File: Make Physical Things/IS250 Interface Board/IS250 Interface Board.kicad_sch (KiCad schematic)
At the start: 6 parts, among them J1 24_Pin_Reorg, J2 16_Pin, J3 Barrel_Jack, SW1 SW_SPST, SW2 SW_MEC_5G

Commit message: Updated Components to have footprints
Added footprints to components that had the wrong ones or were completely missing
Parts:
- J1: footprint (none) -> IS250 Interface Board:24Pin
- J2: footprint (none) -> IS250 Interface Board:16Pin
- J3: footprint (none) -> Connector_BarrelJack:BarrelJack_Horizontal
- SW1: footprint (none) -> IS250 Interface Board:JaycarSlideSwitch
- SW2: footprint (none) -> Button_Switch_THT:SW_Tactile_SPST_Angled_PTS645Vx58-2LFS
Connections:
- net +12V: now also SW1.2 (B); no longer SW1.1 (A)
- net at J1.12 (IGN-SW): now also SW1.1 (A); no longer SW1.2 (B)

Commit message: Added components to PCB
Got all the components adding onto the PCB, and fixed pinname errors with the 2907
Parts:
- XA1: footprint (none) -> Arduino:Arduino_Mega2560_Shield
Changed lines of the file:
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@@
       (effects (font (size 1.524 1.524)))
     )
-    (property "Footprint" "" (id 2) (at 71.12 29.972 0)
+    (property "Footprint" "Arduino:Arduino_Mega2560_Shield" (id 2) (at 71.12 29.972 0)
       (effects (font (size 1.524 1.524)) hide)
     )
@@
     )
     (path "/befd90f1-e350-4c6b-9126-156e7cfd54fd/f532fa97-167c-4bca-bcaf-4a540362fc1c"
-      (reference "RV1") (unit 1) (value "R_Potentiometer") (footprint "")
+      (reference "RV1") (unit 1) (value "R_Potentiometer") (footprint "Potentiometer_THT:Potentiometer_Bourns_3386P_Vertical")
     )
     (path "/67c25448-ea3e-4950-a82a-fe1f009b9ce6"
@@
     )
     (path "/c10fe882-d0c6-4d01-8105-c15a551b4c6b/ee4a6612-4d72-41b2-94a6-c292d4d5cb83"
-      (reference "U2") (unit 1) (value "4017") (footprint "")
+      (reference "U2") (unit 1) (value "4017") (footprint "Package_DIP:DIP-16_W7.62mm")
     )
     (path "/49f3a792-f9d7-417d-ae9d-443f600ad87b"
-      (reference "XA1") (unit 1) (value "Arduino_Mega2560_Shield") (footprint "")
-    )
-  )
+      (reference "XA1") (unit 1) (value "Arduino_Mega2560_Shield") (footprint "Arduino:Arduino_Mega2560_Shield")
+    )
+  )

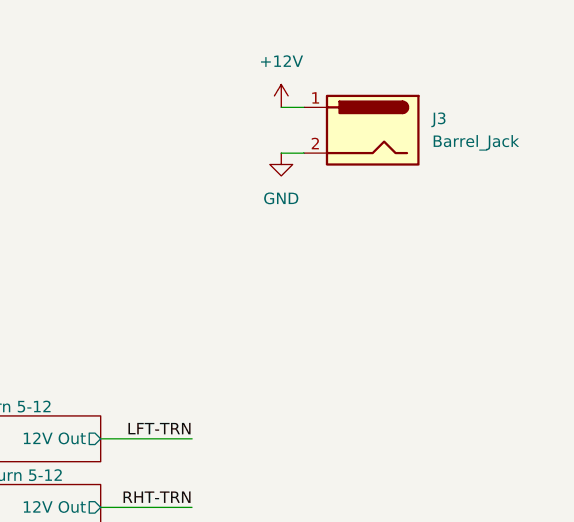
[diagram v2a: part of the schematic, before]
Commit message: Added XT60 and backup fuel resistor
Added an XT60 power connector, and an optional resistor if there isn't an AD8400 connected, so that the fuel gauge will show not empty
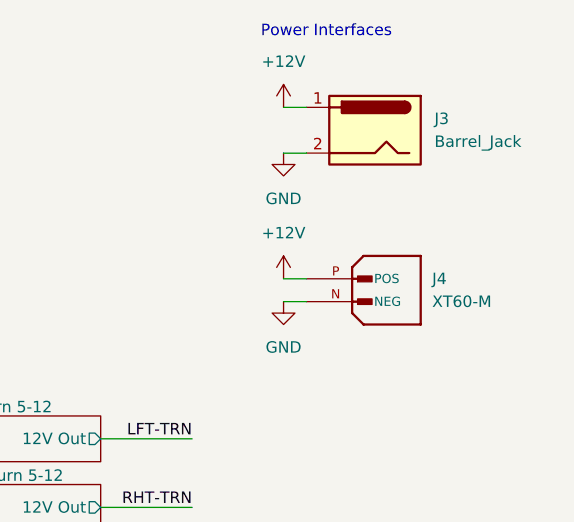
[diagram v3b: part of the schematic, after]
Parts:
- added J4: XT60-M, AMASS_XT60-M, symbol XT60-M:XT60-M
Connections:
- net +12V: now also J4.P (POS)
- net GND: now also J4.N (NEG)
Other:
- note added: "Power Interfaces"
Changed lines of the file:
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@@
-    (stroke (width 0) (type default) (color 0 0 0 0))
-  )
-  (wire (pts (xy 256.286 36.83) (xy 258.826 36.83))
     (stroke (width 0) (type default) (color 0 0 0 0))
   )
@@
     (stroke (width 0) (type default) (color 0 0 0 0))
   )
+  (wire (pts (xy 256.54 36.83) (xy 259.08 36.83))
+    (stroke (width 0) (type default) (color 0 0 0 0))
+  )
   (wire (pts (xy 106.68 60.452) (xy 116.586 60.452))
     (stroke (width 0) (type default) (color 0 0 0 0))
@@
     (stroke (width 0) (type default) (color 0 0 0 0))
   )
-  (wire (pts (xy 256.286 31.75) (xy 258.826 31.75))
+  (wire (pts (xy 256.54 31.75) (xy 259.08 31.75))
     (stroke (width 0) (type default) (color 0 0 0 0))
   )
@@
     (stroke (width 0) (type default) (color 0 0 0 0))
   )
+  (wire (pts (xy 256.54 50.8) (xy 259.08 50.8))
+    (stroke (width 0) (type default) (color 0 0 0 0))
+  )
   (wire (pts (xy 128.778 80.772) (xy 129.794 80.772))
     (stroke (width 0) (type default) (color 0 0 0 0))
@@
     (stroke (width 0) (type default) (color 0 0 0 0))
   )
+  (wire (pts (xy 256.54 53.34) (xy 259.08 53.34))
+    (stroke (width 0) (type default) (color 0 0 0 0))
+  )
   (wire (pts (xy 165.354 70.612) (xy 166.878 70.612))
     (stroke (width 0) (type default) (color 0 0 0 0))
@@
   (wire (pts (xy 121.158 77.47) (xy 121.158 83.566))
     (stroke (width 0) (type default) (color 0 0 0 0))
+  )
+  (text "Power Interfaces\n" (at 254 24.13 0)
+    (effects (font (size 1.27 1.27)) (justify left bottom))
   )
   (label "LFT-T" (at 93.218 116.332 180)
@@
     (effects (font (size 1.27 1.27)) (justify right bottom))
   )
-  (symbol (lib_id "power:+12V") (at 256.286 31.75 0) (unit 1)
-    (in_bom yes) (on_board yes) (fields_autoplaced)
-    (property "Reference" "#PWR0108" (id 0) (at 256.286 35.56 0)
-      (effects (font (size 1.27 1.27)) hide)
-    )
-    (property "Value" "+12V" (id 1) (at 256.286 26.67 0))
-    (property "Footprint" "" (id 2) (at 256.286 31.75 0)
-      (effects (font (size 1.27 1.27)) hide)
-    )
-    (property "Datasheet" "" (id 3) (at 256.286 31.75 0)
+  (symbol (lib_id "power:+12V") (at 256.54 31.75 0) (unit 1)
+    (in_bom yes) (on_board yes) (fields_autoplaced)
+    (property "Reference" "#PWR0108" (id 0) (at 256.54 35.56 0)
+      (effects (font (size 1.27 1.27)) hide)
+    )
+    (property "Value" "+12V" (id 1) (at 256.54 26.67 0))
+    (property "Footprint" "" (id 2) (at 256.54 31.75 0)
+      (effects (font (size 1.27 1.27)) hide)
+    )
+    (property "Datasheet" "" (id 3) (at 256.54 31.75 0)
       (effects (font (size 1.27 1.27)) hide)
     )
@@
     )
     (pin "1")
+  )
+  (symbol (lib_id "XT60-M:XT60-M") (at 264.16 53.34 0) (unit 1)
+    (in_bom yes) (on_board yes) (fields_autoplaced)
+    (property "Reference" "J4" (id 0) (at 273.05 50.7999 0)
+      (effects (font (size 1.27 1.27)) (justify left))
+    )
+    (property "Value" "XT60-M" (id 1) (at 273.05 53.3399 0)
+      (effects (font (size 1.27 1.27)) (justify left))
+    )
+    (property "Footprint" "AMASS_XT60-M" (id 2) (at 264.16 53.34 0)
+      (effects (font (size 1.27 1.27)) (justify left bottom) hide)
+    )
+    (property "Datasheet" "" (id 3) (at 264.16 53.34 0)
+      (effects (font (size 1.27 1.27)) (justify left bottom) hide)
+    )
+    (property "MAXIMUM_PACKAGE_HEIGHT" "16.00 mm" (id 4) (at 264.16 53.34 0)
+      (effects (font (size 1.27 1.27)) (justify left bottom) hide)
+    )
+    (property "MANUFACTURER" "AMASS" (id 5) (at 264.16 53.34 0)
+      (effects (font (size 1.27 1.27)) (justify left bottom) hide)
+    )
+    (property "PARTREV" "V1.2" (id 6) (at 264.16 53.34 0)
+      (effects (font (size 1.27 1.27)) (justify left bottom) hide)
+    )
+    (property "STANDARD" "IPC 7351B" (id 7) (at 264.16 53.34 0)
+      (effects (font (size 1.27 1.27)) (justify left bottom) hide)
+    )
+    (pin "N")
+    (pin "P")
   )
   (symbol (lib_id "Switch:SW_MEC_5G") (at 177.038 85.852 0) (unit 1)
@@
     (pin "2")
   )
-  (symbol (lib_id "power:GND") (at 256.286 36.83 0) (unit 1)
-    (in_bom yes) (on_board yes) (fields_autoplaced)
-    (property "Reference" "#PWR0107" (id 0) (at 256.286 43.18 0)
-      (effects (font (size 1.27 1.27)) hide)
-    )
-    (property "Value" "GND" (id 1) (at 256.286 41.91 0))
-    (property "Footprint" "" (id 2) (at 256.286 36.83 0)
-      (effects (font (size 1.27 1.27)) hide)
-    )
-    (property "Datasheet" "" (id 3) (at 256.286 36.83 0)
-      (effects (font (size 1.27 1.27)) hide)
-    )
-    (pin "1")
-  )
-  (symbol (lib_id "Connector:Barrel_Jack") (at 266.446 34.29 0) (mirror y) (unit 1)
-    (in_bom yes) (on_board yes) (fields_autoplaced)
-    (property "Reference" "J3" (id 0) (at 273.05 33.0199 0)
-      (effects (font (size 1.27 1.27)) (justify right))
-    )
-    (property "Value" "Barrel_Jack" (id 1) (at 273.05 35.5599 0)
-      (effects (font (size 1.27 1.27)) (justify right))
-    )
-    (property "Footprint" "Connector_BarrelJack:BarrelJack_Horizontal" (id 2) (at 265.176 35.306 0)
-      (effects (font (size 1.27 1.27)) hide)
-    )
-    (property "Datasheet" "~" (id 3) (at 265.176 35.306 0)
+  (symbol (lib_id "power:GND") (at 256.54 53.34 0) (unit 1)
+    (in_bom yes) (on_board yes) (fields_autoplaced)
+    (property "Reference" "#PWR0133" (id 0) (at 256.54 59.69 0)
+      (effects (font (size 1.27 1.27)) hide)
+    )
+    (property "Value" "GND" (id 1) (at 256.54 58.42 0))
+    (property "Footprint" "" (id 2) (at 256.54 53.34 0)
+      (effects (font (size 1.27 1.27)) hide)
+    )
+    (property "Datasheet" "" (id 3) (at 256.54 53.34 0)
+      (effects (font (size 1.27 1.27)) hide)
+    )
+    (pin "1")
+  )
+  (symbol (lib_id "power:GND") (at 256.54 36.83 0) (unit 1)
+    (in_bom yes) (on_board yes) (fields_autoplaced)
+    (property "Reference" "#PWR0107" (id 0) (at 256.54 43.18 0)
+      (effects (font (size 1.27 1.27)) hide)
+    )
+    (property "Value" "GND" (id 1) (at 256.54 41.91 0))
+    (property "Footprint" "" (id 2) (at 256.54 36.83 0)
+      (effects (font (size 1.27 1.27)) hide)
+    )
+    (property "Datasheet" "" (id 3) (at 256.54 36.83 0)
+      (effects (font (size 1.27 1.27)) hide)
+    )
+    (pin "1")
+  )
+  (symbol (lib_id "power:+12V") (at 256.54 50.8 0) (unit 1)
+    (in_bom yes) (on_board yes) (fields_autoplaced)
+    (property "Reference" "#PWR0134" (id 0) (at 256.54 54.61 0)
+      (effects (font (size 1.27 1.27)) hide)
+    )
+    (property "Value" "+12V" (id 1) (at 256.54 45.72 0))
+    (property "Footprint" "" (id 2) (at 256.54 50.8 0)
+      (effects (font (size 1.27 1.27)) hide)
+    )
+    (property "Datasheet" "" (id 3) (at 256.54 50.8 0)
+      (effects (font (size 1.27 1.27)) hide)
+    )
+    (pin "1")
+  )
+  (symbol (lib_id "Connector:Barrel_Jack") (at 266.7 34.29 0) (mirror y) (unit 1)
+    (in_bom yes) (on_board yes) (fields_autoplaced)
+    (property "Reference" "J3" (id 0) (at 273.304 33.0199 0)
+      (effects (font (size 1.27 1.27)) (justify right))
+    )
+    (property "Value" "Barrel_Jack" (id 1) (at 273.304 35.5599 0)
+      (effects (font (size 1.27 1.27)) (justify right))
+    )
+    (property "Footprint" "Connector_BarrelJack:BarrelJack_Horizontal" (id 2) (at 265.43 35.306 0)
+      (effects (font (size 1.27 1.27)) hide)
+    )
+    (property "Datasheet" "~" (id 3) (at 265.43 35.306 0)
       (effects (font (size 1.27 1.27)) hide)
     )
@@
       (reference "#PWR0132") (unit 1) (value "+12V") (footprint "")
     )
+    (path "/6a6f2c78-ccc0-41fa-beba-1d8264551389"
+      (reference "#PWR0133") (unit 1) (value "GND") (footprint "")
+    )
+    (path "/8595ee52-f88c-4dfe-a3e8-64a4bc6cf3ba"
+      (reference "#PWR0134") (unit 1) (value "+12V") (footprint "")
+    )
     (path "/b4ad7ea6-c60f-4c23-983b-e568869cc5ae"
       (reference "J1") (unit 1) (value "24_Pin_Reorg") (footprint "IS250 Interface Board:24Pin")
@@
       (reference "J3") (unit 1) (value "Barrel_Jack") (footprint "Connector_BarrelJack:BarrelJack_Horizontal")
     )
+    (path "/31965dda-df71-4f19-aaa7-a9c32fd53870"
+      (reference "J4") (unit 1) (value "XT60-M") (footprint "AMASS_XT60-M")
+    )
     (path "/4f921d5d-474a-4419-8896-2f1daac616ec/656b042d-303f-4221-8f97-e16356b26f03"
       (reference "Q1") (unit 1) (value "PN2222A") (footprint "Package_TO_SOT_THT:TO-92_Inline")
@@
       (reference "R18") (unit 1) (value "22k") (footprint "Resistor_THT:R_Axial_DIN0207_L6.3mm_D2.5mm_P10.16mm_Horizontal")
     )
+    (path "/fb4c306c-6f15-4891-a6a0-0fc209f21aff/2d6b81de-5cb3-4023-a003-a5926a13669f"
+      (reference "R19") (unit 1) (value "100") (footprint "Resistor_THT:R_Axial_DIN0207_L6.3mm_D2.5mm_P10.16mm_Horizontal")
+    )
     (path "/befd90f1-e350-4c6b-9126-156e7cfd54fd/f532fa97-167c-4bca-bcaf-4a540362fc1c"

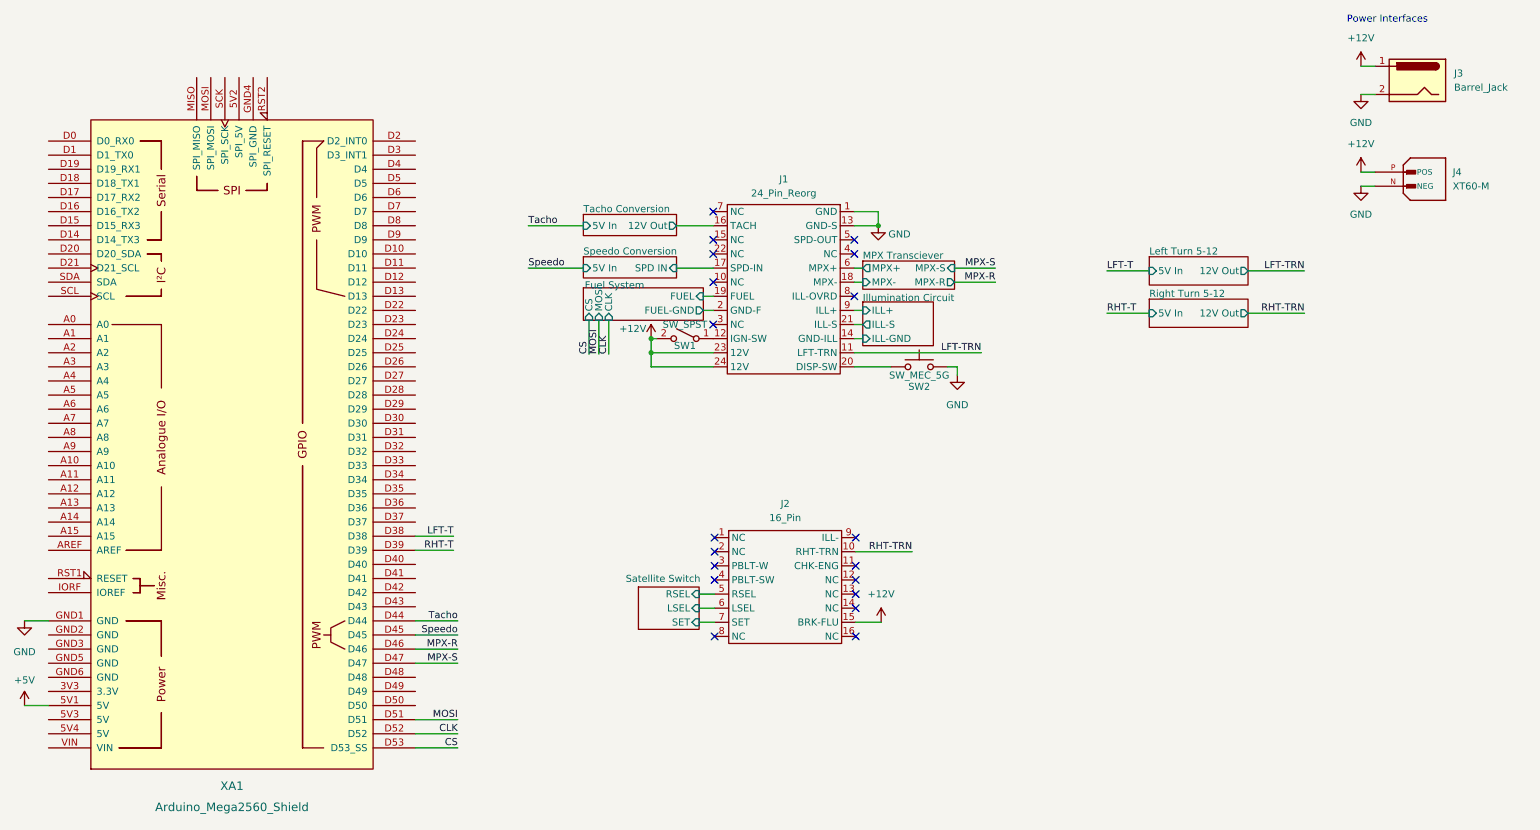
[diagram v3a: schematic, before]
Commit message: Added Reset Circuit
Added a button to allow you to reset the arduino, if it decides to die. Also fixed the footprints for the buttons so that they actually function as buttons.
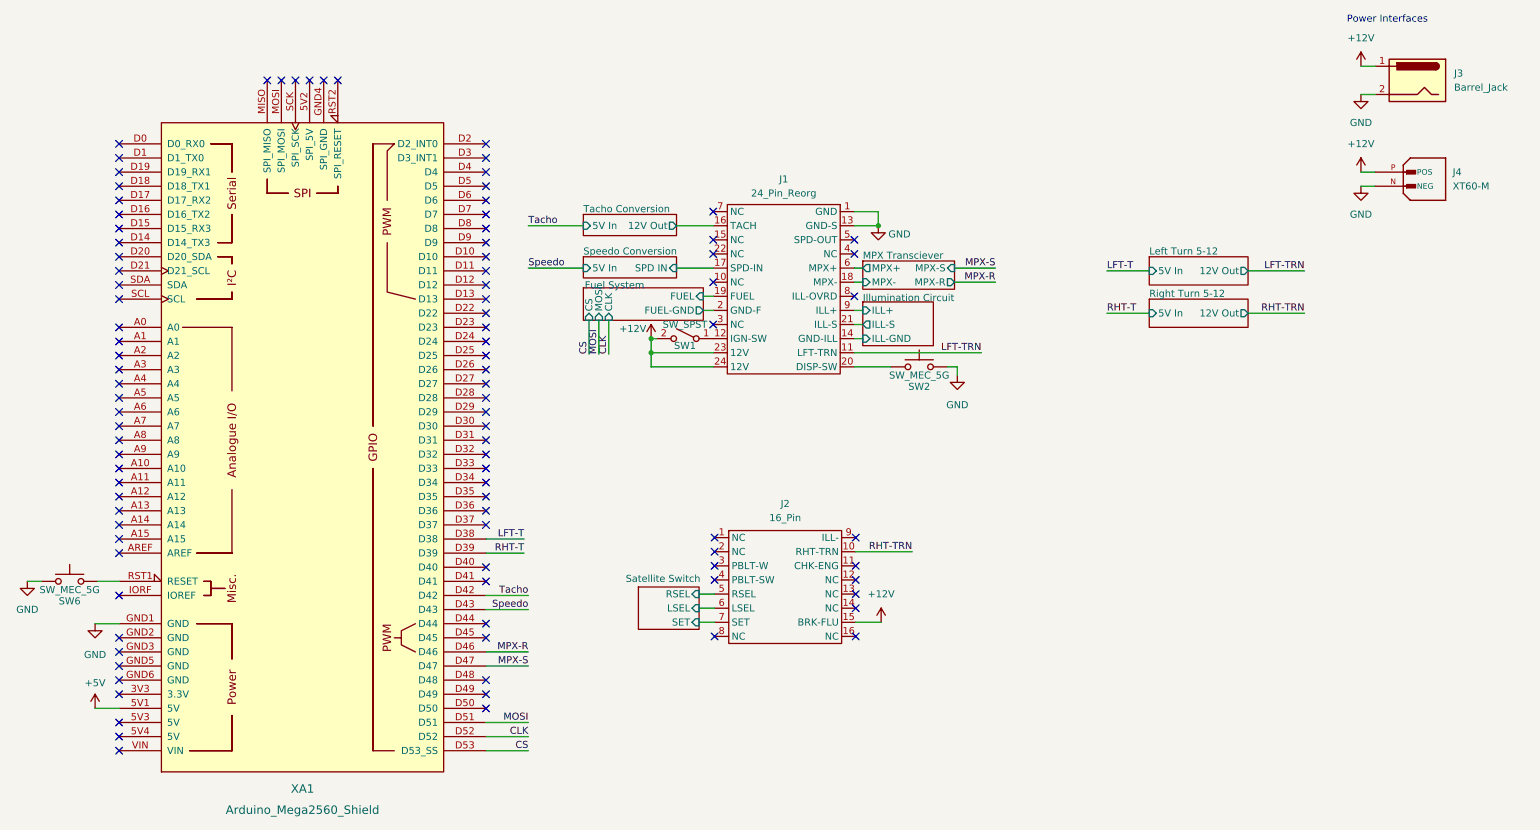
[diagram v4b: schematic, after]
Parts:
- added SW6: SW_MEC_5G, Button_Switch_THT:SW_Tactile_SPST_Angled_PTS645Vx58-2LFS, symbol Switch:SW_MEC_5G
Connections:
- net GND: now also SW2.1 (A), SW2.2 (A), SW6.2 (A), SW6.4 (B); no longer SW2.3 (B), SW2.4 (B)
- net Speedo: now also XA1.D43; no longer XA1.D45
- net Tacho: now also XA1.D42; no longer XA1.D44
- net at XA1.RST1 (RESET): now also SW6.1 (A), SW6.2 (A)
- new net: J1.20 (DISP-SW), SW2.3 (B), SW2.4 (B)
- no-connect marks 19 -> 98
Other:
- moved on the sheet: XA1
